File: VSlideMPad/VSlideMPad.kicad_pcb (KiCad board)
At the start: 2 copper layers, 4 parts

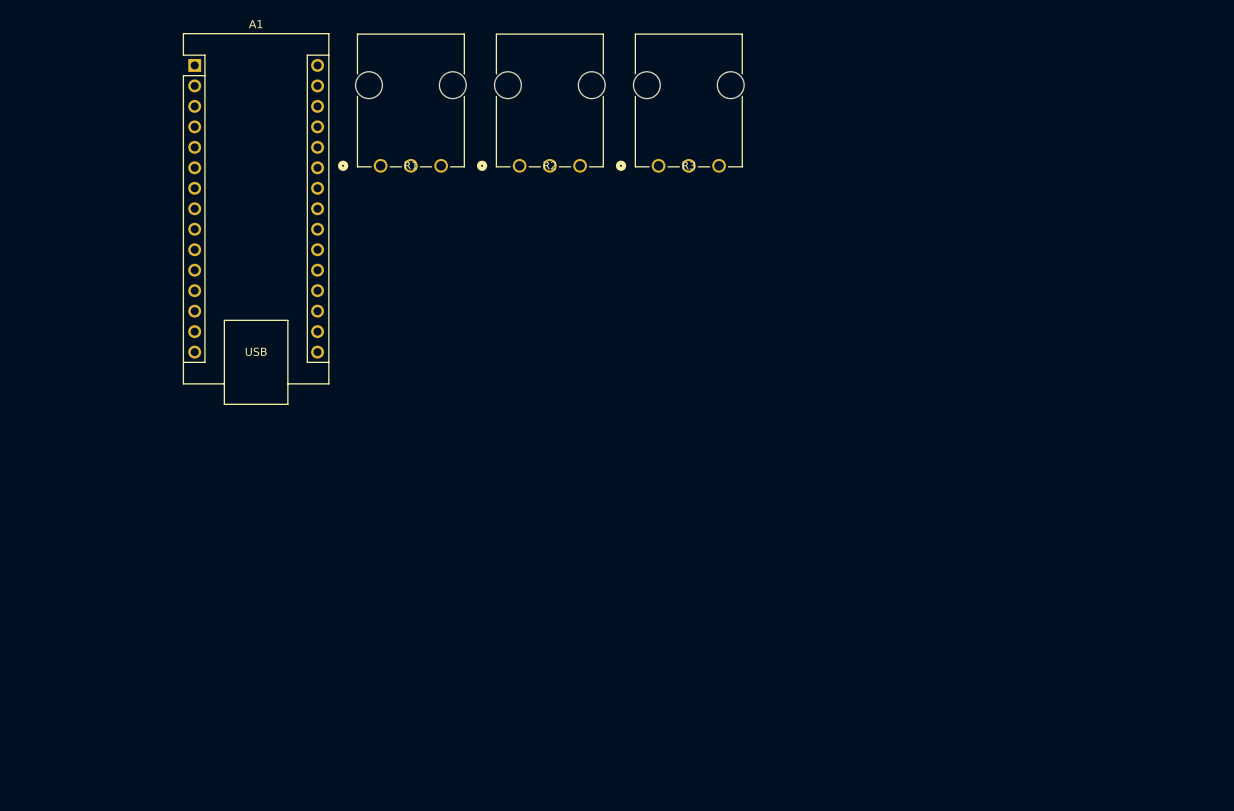
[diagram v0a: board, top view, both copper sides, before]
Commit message: fixed added cherry switches and fixed potentiometres
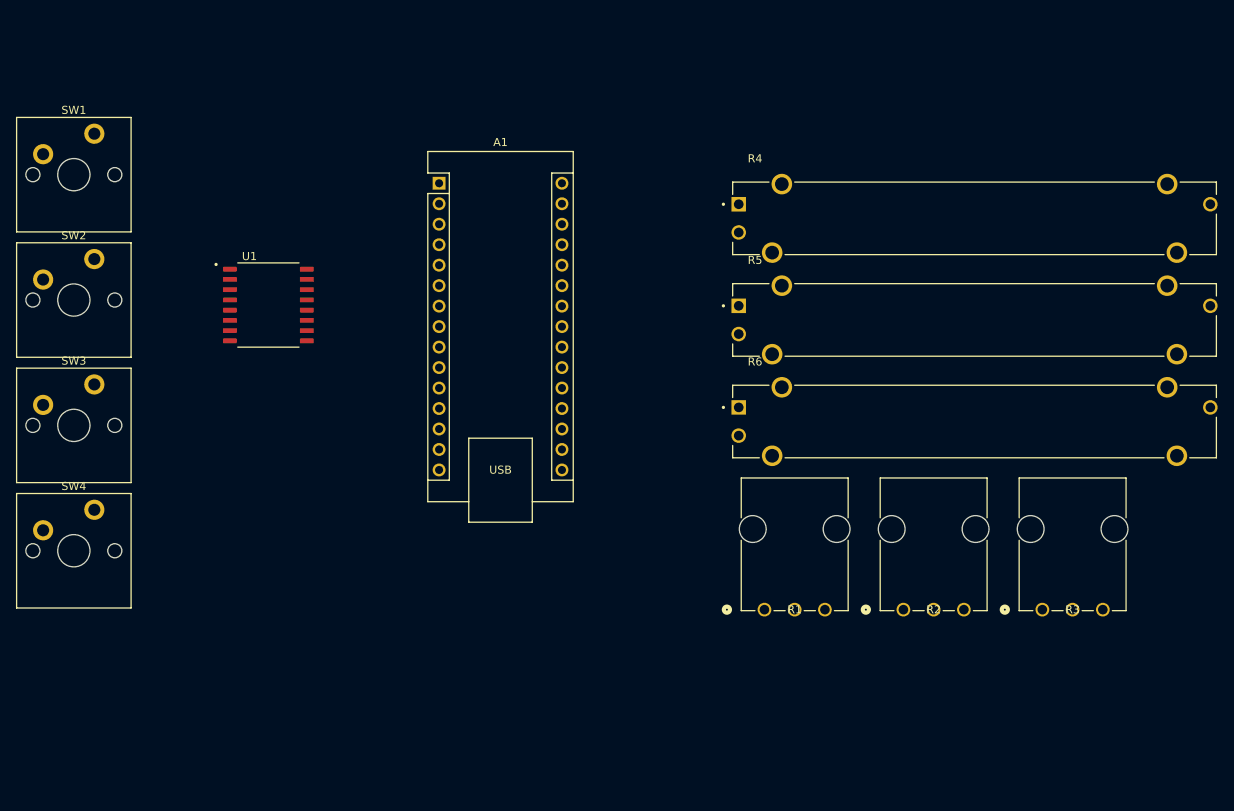
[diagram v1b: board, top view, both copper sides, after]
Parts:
- added R4: PTA4543-2015DPB103, PTA4543-2015DPB103:TRIM_PTA4543-2015DPB103, F.Cu at (176.5, 62.9)
- added R5: PTA4543-2015DPB103, PTA4543-2015DPB103:TRIM_PTA4543-2015DPB103, F.Cu at (176.5, 75.5)
- added R6: PTA4543-2015DPB103, PTA4543-2015DPB103:TRIM_PTA4543-2015DPB103, F.Cu at (176.5, 88.1)
- added SW1: SW_Push, Switch_Keyboard_Cherry_MX:SW_Cherry_MX_PCB_1.00u, F.Cu at (64.8, 57.5)
- added SW2: SW_Push, Switch_Keyboard_Cherry_MX:SW_Cherry_MX_PCB_1.00u, F.Cu at (64.8, 73.0)
- added SW3: SW_Push, Switch_Keyboard_Cherry_MX:SW_Cherry_MX_PCB_1.00u, F.Cu at (64.8, 88.6)
- added SW4: SW_Push, Switch_Keyboard_Cherry_MX:SW_Cherry_MX_PCB_1.00u, F.Cu at (64.8, 104.1)
- added U1: MC14490DWG, MC14490DWG:SOIC127P1030X265-16N, F.Cu at (88.9, 73.7)
- R1, R2, R3: footprint VSlideMPad:POT_P120PK-x25_TTE -> POT_P120PK-x25_TTE:POT_P120PK-x25_TTE
- moved R1 72.8 mm to (150.4, 111.4)
- moved R2 72.8 mm to (167.7, 111.4)
- moved R3 72.8 mm to (184.9, 111.4)
- moved A1 33.7 mm to (110.1, 58.6)
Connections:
- A1 pad 11: unconnected-(A1-D8-Pad11) -> Net-(A1-D8)
- A1 pad 19: unconnected-(A1-A0-Pad19) -> Net-(A1-A0)
- A1 pad 20: unconnected-(A1-A1-Pad20) -> Net-(A1-A1)
- A1 pad 21: unconnected-(A1-A2-Pad21) -> Net-(A1-A2)
- A1 pad 22: unconnected-(A1-A3-Pad22) -> Net-(A1-A3)
- A1 pad 23: unconnected-(A1-A4-Pad23) -> Net-(A1-A4)
- A1 pad 24: unconnected-(A1-A5-Pad24) -> Net-(A1-A5)
- A1 pad 5: unconnected-(A1-D2-Pad5) -> Net-(A1-D2)
- A1 pad 6: unconnected-(A1-D3-Pad6) -> Net-(A1-D3)
- A1 pad 7: unconnected-(A1-D4-Pad7) -> Net-(A1-D4)
- A1 pad 8: unconnected-(A1-D5-Pad8) -> Net-(A1-D5)
- R1 pad 1: unconnected-(R1-Pad1) -> +5V
- R1 pad 2: unconnected-(R1-Pad2) -> Net-(A1-A0)
- R1 pad 3: unconnected-(R1-Pad3) -> GND
- R2 pad 1: unconnected-(R2-Pad1) -> +5V
- R2 pad 2: unconnected-(R2-Pad2) -> Net-(A1-A1)
- R2 pad 3: unconnected-(R2-Pad3) -> GND
- R3 pad 1: unconnected-(R3-Pad1) -> +5V
- R3 pad 2: unconnected-(R3-Pad2) -> Net-(A1-A2)
- R3 pad 3: unconnected-(R3-Pad3) -> GND

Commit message: board layout v1
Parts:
- A1, U1: moved to B.Cu
- moved R4 67.9 mm to (110.5, 78.7), turned to 90 degrees
- moved R5 51.6 mm to (124.9, 78.7), turned to 90 degrees
- moved R3 48.3 mm to (139.4, 127.6)
- moved R2 47.6 mm to (122.9, 127.6)
- moved R1 46.9 mm to (106.4, 127.6)
- moved R6 37.5 mm to (140.2, 78.7), turned to 90 degrees
- moved U1 35.3 mm to (116.8, 95.2), turned to 180 degrees
- moved SW4 29.5 mm to (91.4, 116.8)
- moved SW3 27.8 mm to (91.4, 96.5)
- moved SW2 26.9 mm to (91.4, 76.8)
- moved SW1 26.7 mm to (91.4, 57.1)
- moved A1 25.3 mm to (110.5, 83.8)
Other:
- board outline added: 73.7 x 87.6 mm

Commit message: v1 routage
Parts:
- moved A1 1.18 mm to (111.4, 83.0)
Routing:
- net GND: track 0.00 -> 251.9 mm, vias 0 -> 1
- net +5V: track 0.00 -> 135.0 mm, vias 0 -> 1
- net Net-(A1-A0): track 0.00 -> 79.6 mm
- net Net-(A1-A2): track 0.00 -> 74.3 mm
- net Net-(A1-A1): track 0.00 -> 74.1 mm
- net Net-(U1-AIN): track 0.00 -> 66.3 mm, vias 0 -> 1
- net Net-(A1-A3): track 0.00 -> 55.1 mm, vias 0 -> 1
- net Net-(A1-A4): track 0.00 -> 53.4 mm
- net Net-(A1-A5): track 0.00 -> 51.7 mm, vias 0 -> 1
- net Net-(A1-D8): track 0.00 -> 46.7 mm, vias 0 -> 1
- net Net-(U1-BIN): track 0.00 -> 38.5 mm, vias 0 -> 1
- net Net-(U1-CIN): track 0.00 -> 37.9 mm
- net Net-(A1-D5): track 0.00 -> 37.3 mm, vias 0 -> 1
- net Net-(A1-D3): track 0.00 -> 30.2 mm, vias 0 -> 1
- net Net-(A1-D4): track 0.00 -> 30.1 mm, vias 0 -> 1
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
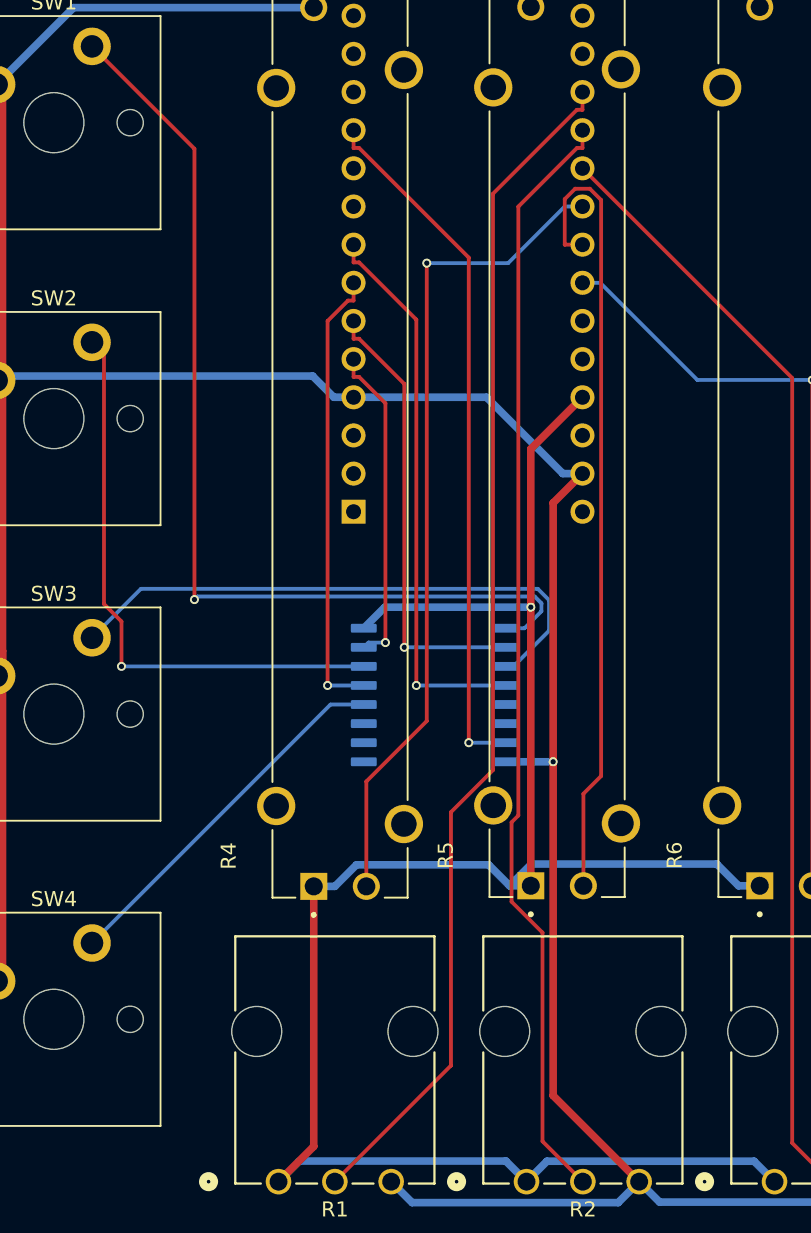
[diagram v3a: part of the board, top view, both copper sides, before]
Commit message: ajout cap mc44040
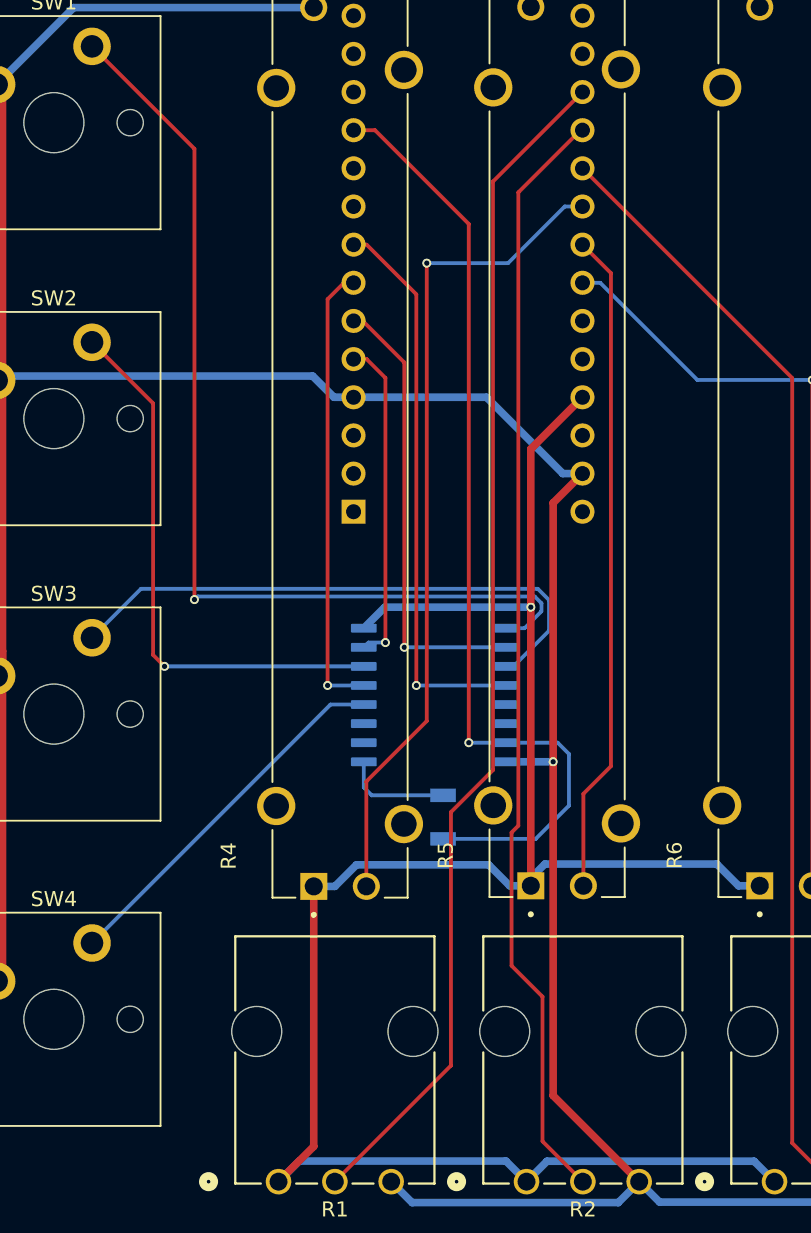
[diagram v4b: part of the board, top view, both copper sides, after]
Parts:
- added C1: 10n, 4ms_Capacitor:C_1206, B.Cu at (117.3, 103.4)
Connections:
- A1 pad 11: Net-(A1-D8) -> unconnected-(A1-D8-Pad11)
- U1 pad 7: Net-(A1-D8) -> Net-(C1-+)
- U1 pad 9: unconnected-(U1-OSCOUT-Pad9) -> Net-(C1--)
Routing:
- net (no net): track 0.00 -> 47.3 mm, vias 0 -> 1
- net Net-(A1-D8): track 46.7 -> 0.00 mm, vias 1 -> 0
- net Net-(C1-+): track 0.00 -> 16.7 mm
- net Net-(A1-A4): track 53.4 -> 44.2 mm
- net Net-(C1--): track 0.00 -> 7.20 mm
- net Net-(U1-BIN): track 38.5 -> 36.8 mm
- net +5V: track 135.0 -> 133.9 mm

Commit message: Small layout change
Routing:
- added copper zone on B.Cu, net GND
- added copper zone on F.Cu, net GND
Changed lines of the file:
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@@
 		(net 39)
+	)
+	(zone
+		(net 8)
+		(net_name "GND")
+		(layers "F.Cu" "B.Cu")
+		(name "Ground plane")
+		(hatch edge 0.5)
+		(connect_pads
+			(clearance 0.5)
+		)
+		(min_thickness 0.25)
+		(filled_areas_thickness no)
+		(fill yes
+			(thermal_gap 0.5)
+			(thermal_bridge_width 0.5)
+		)
+		(polygon
+			(pts
+				(xy 76.97456 42.926) (xy 76.97456 42.926) (xy 155.448 42.926) (xy 156.718 134.112) (xy 75.184 134.366)
+				(xy 76.2 89.916)
+			)
+		)
 	)
 	(embedded_fonts no)

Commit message: V1 FABRICATED
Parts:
- added TP1: +5V, 4ms_TestPoint:TestPoint_Pad_06, F.Cu at (132.6, 75.4)
- added TP2: GND, 4ms_TestPoint:TestPoint_Pad_06, F.Cu at (132.6, 80.5)
- C1: value 10n -> 6.7n
- moved C1 0.25 mm to (117.6, 103.4)
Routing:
- net (no net): track 47.3 -> 0.00 mm, vias 1 -> 0
- net GND: track 251.9 -> 257.9 mm, vias 1 -> 8
- net +5V: track 133.9 -> 139.9 mm
- net Net-(A1-A4): track 44.2 -> 49.7 mm
- net Net-(A1-A1): track 74.0 -> 74.6 mm
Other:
- board size 73.7 x 87.6 mm -> 82 x 88.6 mm
- board text added: "JLCJLCJLCJLC"
- board text added: "Made By Arballio, Montréal"
- board text added: "Volume Slider and Macro Pad (VSMP-V1)"
